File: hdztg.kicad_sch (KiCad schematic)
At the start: 8 parts, among them J1 20374-R20E-31, Q1 2N7002KDW 72K

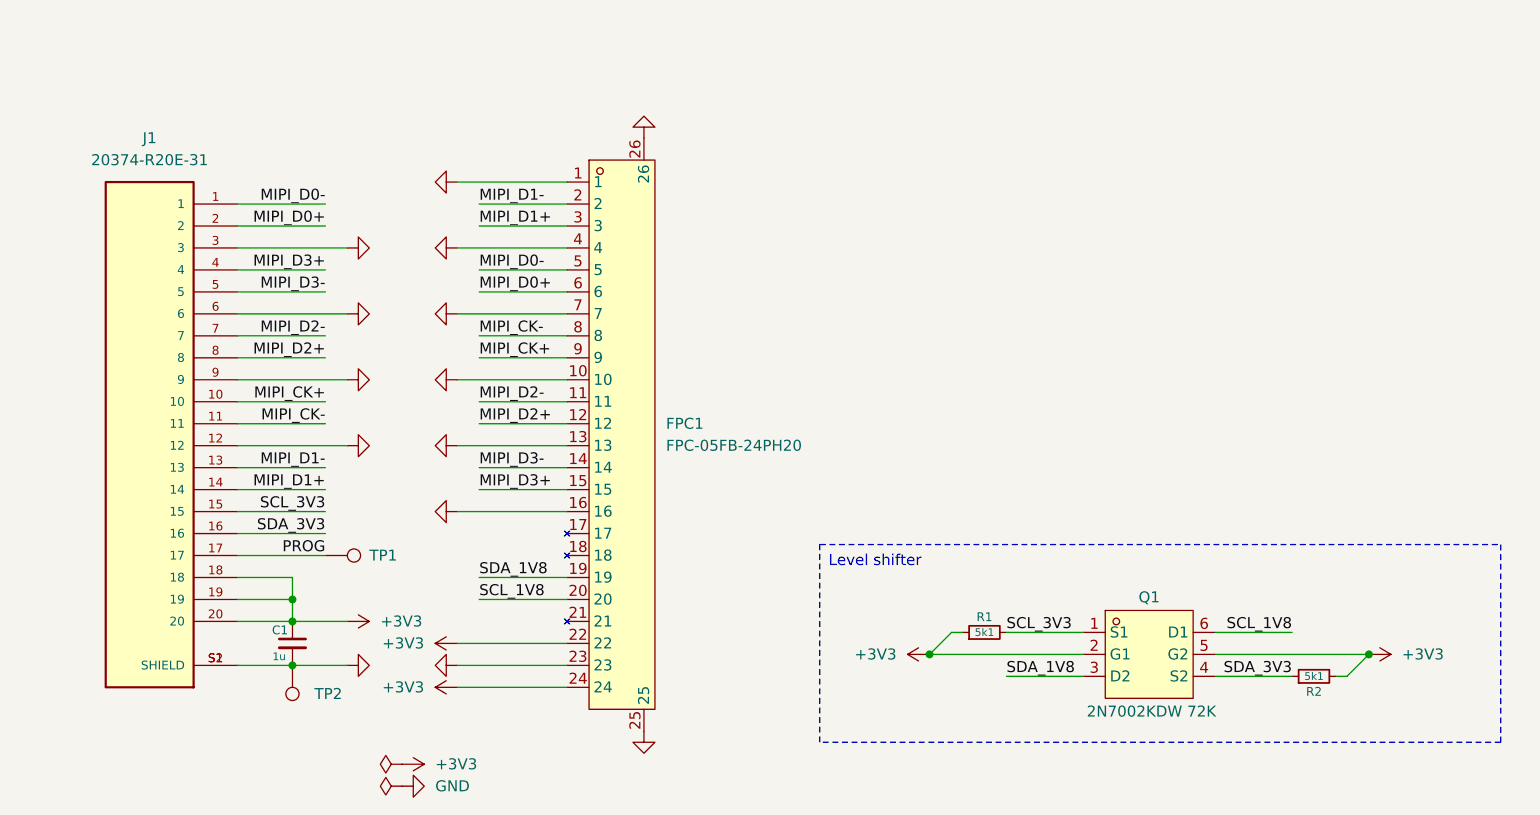
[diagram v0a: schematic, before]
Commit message: update pcb, fix level shifter
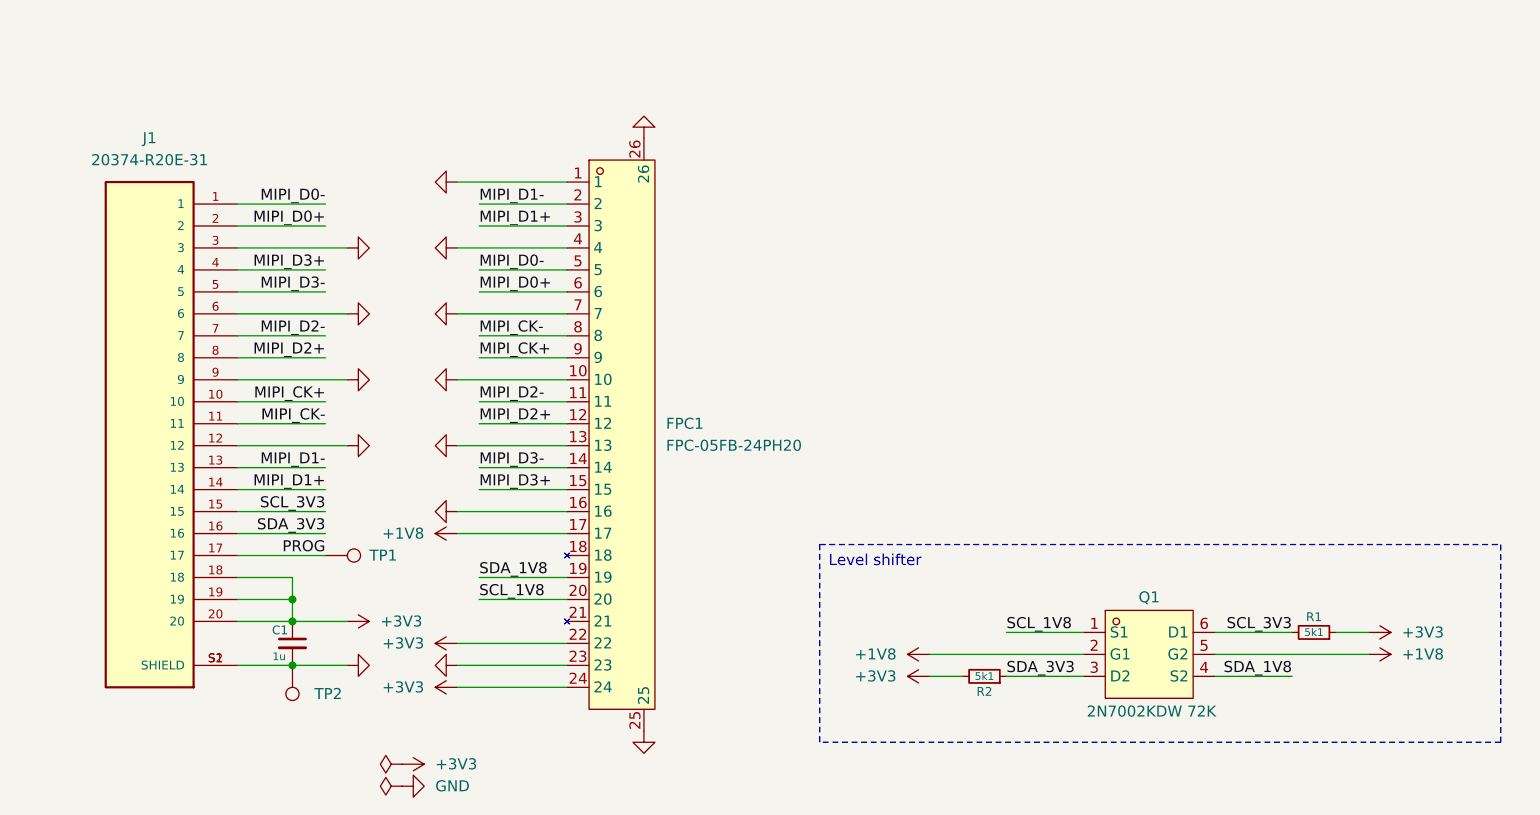
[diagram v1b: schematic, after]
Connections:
- net +3V3: no longer Q1.2 (G1), Q1.5 (G2)
- net SCL_1V8: now also Q1.1 (S1); no longer Q1.6 (D1)
- net SCL_3V3: now also Q1.6 (D1); no longer Q1.1 (S1)
- net SDA_1V8: now also Q1.4 (S2); no longer Q1.3 (D2)
- net SDA_3V3: now also Q1.3 (D2); no longer Q1.4 (S2)
- net +1V8: now reaches FPC1.17
- net +1V8: now also Q1.2 (G1), Q1.5 (G2)
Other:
- moved on the sheet: R1, R2

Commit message: update pcb
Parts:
- FPC1: Manufacturer Part (none) -> FPC-05FB-24PH20; Supplier Link (none) -> https://lcsc.com/product-detail/FFC-FPC-Flat-Flexible-Conne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
- J1: Availability In Stock -> (none); Check_prices https://www.snapeda.com/parts/20374-R20E-31/I-PEX/view-part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 -> (none); Description_1 20 POS Right Angle SMD 0.4 mm pitch vertical mating type mi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 -> (none); DigiKey Part (none) -> 5378-20374-R20E-31TR-ND; MANUFACTURER I-PEX -> (none); MF I-PEX -> (none); MP 20374-R20E-31 -> (none); Manufacturer (none) -> I-PEX; Manufacturer Product Number (none) -> 20374-R20E-31; PARTREV 24 -> (none); Package None -> (none); Price None -> (none); STANDARD Manufacturer Recommendation -> (none); SnapEDA_Link https://www.snapeda.com/parts/20374-R20E-31/I-PEX/view-part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 -> (none); Supplier Link (none) -> https://www.digikey.com/en/products/detail/i-pex/20374-R20E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
- Q1: Manufacturer Part (none) -> 2N7002KDW; Supplier Link (none) -> https://lcsc.com/product-detail/MOSFETs_CBI-2N7002KDW_C2919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
- R1, R2: LCSC Part (none) -> C274341; Manufacturer Part (none) -> RC0201FR-075K1L; Supplier Link (none) -> https://lcsc.com/product-detail/Chip-Resistor-Surface-Mount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
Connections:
- net +3V3: now also R1.2; no longer R1.1
- net SCL_3V3: now also R1.1; no longer R1.2
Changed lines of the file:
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@@
 			)
 		)
-		(property "Datasheet" ""
+		(property "Datasheet" "https://www.i-pex.com/sites/default/files/downloads/pdf/CATALOG_CABLINE-SS_E.pdf"
 			(at 35.56 62.23 0)
 			(effects
@@
 			)
 		)
-		(property "Description" ""
+		(property "Description" "20 POS Right Angle SMD 0.4 mm pitch vertical mating type micro-coaxial connector with friction lock CABLINE SS Receptacle"
 			(at 35.56 62.23 0)
 			(effects
@@
 			)
 		)
-		(property "MF" "I-PEX"
+		(property "Manufacturer Product Number" "20374-R20E-31"
 			(at 35.56 62.23 0)
 			(effects
@@
 			)
 		)
-		(property "Description_1" "20 POS Right Angle SMD 0.4 mm pitch vertical mating type micro-coaxial connector with friction lock CABLINE SS Receptacle"
+		(property "Manufacturer" "I-PEX"
 			(at 35.56 62.23 0)
 			(effects
@@
 			)
 		)
-		(property "Package" "None"
+		(property "DigiKey Part" "5378-20374-R20E-31TR-ND"
 			(at 35.56 62.23 0)
 			(effects
@@
 					(size 1.27 1.27)
 				)
-				(justify bottom)
-				(hide yes)
-			)
-		)
-		(property "Price" "None"
+				(hide yes)
+			)
+		)
+		(property "Supplier Link" "https://www.digikey.com/en/products/detail/i-pex/20374-R20E-31/24394701"
 			(at 35.56 62.23 0)
 			(effects
@@
 					(size 1.27 1.27)
 				)
-				(justify bottom)
-				(hide yes)
-			)
-		)
-		(property "Check_prices" "https://www.snapeda.com/parts/20374-R20E-31/I-PEX/view-part/?ref=eda"
-			(at 35.56 62.23 0)
-			(effects
-				(font
-					(size 1.27 1.27)
-				)
-				(justify bottom)
-				(hide yes)
-			)
-		)
-		(property "STANDARD" "Manufacturer Recommendation"
-			(at 35.56 62.23 0)
-			(effects
-				(font
-					(size 1.27 1.27)
-				)
-				(justify bottom)
-				(hide yes)
-			)
-		)
-		(property "PARTREV" "24"
-			(at 35.56 62.23 0)
-			(effects
-				(font
-					(size 1.27 1.27)
-				)
-				(justify bottom)
-				(hide yes)
-			)
-		)
-		(property "SnapEDA_Link" "https://www.snapeda.com/parts/20374-R20E-31/I-PEX/view-part/?ref=snap"
-			(at 35.56 62.23 0)
-			(effects
-				(font
-					(size 1.27 1.27)
-				)
-				(justify bottom)
-				(hide yes)
-			)
-		)
-		(property "MP" "20374-R20E-31"
-			(at 35.56 62.23 0)
-			(effects
-				(font
-					(size 1.27 1.27)
-				)
-				(justify bottom)
-				(hide yes)
-			)
-		)
-		(property "Availability" "In Stock"
-			(at 35.56 62.23 0)
-			(effects
-				(font
-					(size 1.27 1.27)
-				)
-				(justify bottom)
-				(hide yes)
-			)
-		)
-		(property "MANUFACTURER" "I-PEX"
-			(at 35.56 62.23 0)
-			(effects
-				(font
-					(size 1.27 1.27)
-				)
-				(justify bottom)
 				(hide yes)
 			)
@@
 			)
 		)
+		(property "Manufacturer Part" "2N7002KDW"
+			(at 151.13 88.9 0)
+			(effects
+				(font
+					(size 1.27 1.27)
+				)
+				(hide yes)
+			)
+		)
 		(property "LCSC Part" "C2919800"
 			(at 151.13 101.6 0)
+			(effects
+				(font
+					(size 1.27 1.27)
+				)
+				(hide yes)
+			)
+		)
+		(property "Supplier Link" "https://lcsc.com/product-detail/MOSFETs_CBI-2N7002KDW_C2919800.html?s_z=n_2N7002KDW"
+			(at 151.13 88.9 0)
 			(effects
 				(font
@@
 	)
 	(symbol
+		(lib_id "Device:R_Small")
+		(at 170.18 86.36 90)
+		(mirror x)
+		(unit 1)
+		(exclude_from_sim no)
+		(in_bom yes)
+		(on_board yes)
+		(dnp no)
+		(property "Reference" "R1"
+			(at 170.18 84.582 90)
+			(effects
+				(font
+					(size 1.016 1.016)
+				)
+			)
+		)
+		(property "Value" "5k1"
+			(at 170.18 86.36 90)
+			(effects
+				(font
+					(size 0.889 0.889)
+				)
+			)
+		)
+		(property "Footprint" "Resistor_SMD:R_0201_0603Metric"
+			(at 170.18 86.36 0)
+			(effects
+				(font
+					(size 1.27 1.27)
+				)
+				(hide yes)
+			)
+		)
+		(property "Datasheet" "https://lcsc.com/datasheet/lcsc_datasheet_2506161045_YAGEO-RC0201FR-075K1L_C274341.pdf"
+			(at 170.18 86.36 0)
+			(effects
+				(font
+					(size 1.27 1.27)
+				)
+				(hide yes)
+			)
+		)
+		(property "Description" "Resistor, small symbol"
+			(at 170.18 86.36 0)
+			(effects
+				(font
+					(size 1.27 1.27)
+				)
+				(hide yes)
+			)
+		)
+		(property "Manufacturer Part" "RC0201FR-075K1L"
+			(at 170.18 86.36 90)
+			(effects
+				(font
+					(size 1.27 1.27)
+				)
+				(hide yes)
+			)
+		)
+		(property "LCSC Part" "C274341"
+			(at 170.18 86.36 90)
+			(effects
+				(font
+					(size 1.27 1.27)
+				)
+				(hide yes)
+			)
+		)
+		(property "Supplier Link" "https://lcsc.com/product-detail/Chip-Resistor-Surface-Mount_YAGEO-RC0201FR-075K1L_C274341.html"
+			(at 170.18 86.36 90)
+			(effects
+				(font
+					(size 1.27 1.27)
+				)
+				(hide yes)
+			)
+		)
+		(pin "1"
+		)
+		(pin "2"
+		)
+		(instances
+			(project "hdztg"
+				(path "/5fa3be86-0836-40c5-8497-58cbc35ea59a"
+					(reference "R1")
+					(unit 1)
+				)
+			)
+		)
+	)
+	(symbol
 		(lib_id "power:GND")
 		(at 58.42 41.91 90)
@@
 				(path "/5fa3be86-0836-40c5-8497-58cbc35ea59a"
 					(reference "#PWR015")
-					(unit 1)
-				)
-			)
-		)
-	)
-	(symbol
-		(lib_id "Device:R_Small")
-		(at 170.18 86.36 270)
-		(mirror x)
-		(unit 1)
-		(exclude_from_sim no)
-		(in_bom yes)
-		(on_board yes)
-		(dnp no)
-		(property "Reference" "R1"
-			(at 170.18 84.582 90)
-			(effects
-				(font
-					(size 1.016 1.016)
-				)
-			)
-		)
-		(property "Value" "5k1"
-			(at 170.18 86.36 90)
-			(effects
-				(font
-					(size 0.889 0.889)
-				)
-			)
-		)
-		(property "Footprint" "Resistor_SMD:R_0201_0603Metric"
-			(at 170.18 86.36 0)
-			(effects
-				(font
-					(size 1.27 1.27)
-				)
-				(hide yes)
-			)
-		)
-		(property "Datasheet" "~"
-			(at 170.18 86.36 0)
-			(effects
-				(font
-					(size 1.27 1.27)
-				)
-				(hide yes)
-			)
-		)
-		(property "Description" "Resistor, small symbol"
-			(at 170.18 86.36 0)
-			(effects
-				(font
-					(size 1.27 1.27)
-				)
-				(hide yes)
-			)
-		)
-		(pin "1"
-		)
-		(pin "2"
-		)
-		(instances
-			(project "hdztg"
-				(path "/5fa3be86-0836-40c5-8497-58cbc35ea59a"
-					(reference "R1")
 					(unit 1)
 				)
@@
 			)
 		)
-		(property "Datasheet" "~"
+		(property "Datasheet" "https://lcsc.com/datasheet/lcsc_datasheet_2506161045_YAGEO-RC0201FR-075K1L_C274341.pdf"
 			(at 132.08 91.44 0)
 			(effects
@@
 			)
 		)
+		(property "Manufacturer Part" "RC0201FR-075K1L"
+			(at 132.08 91.44 90)
+			(effects
+				(font
+					(size 1.27 1.27)
+				)
+				(hide yes)
+			)
+		)
+		(property "LCSC Part" "C274341"
+			(at 132.08 91.44 90)
+			(effects
+				(font
+					(size 1.27 1.27)
+				)
+				(hide yes)
+			)
+		)
+		(property "Supplier Link" "https://lcsc.com/product-detail/Chip-Resistor-Surface-Mount_YAGEO-RC0201FR-075K1L_C274341.html"
+			(at 132.08 91.44 90)
+			(effects
+				(font
+					(size 1.27 1.27)
+				)
+				(hide yes)
+			)
+		)
 		(pin "1"
 		)
@@
 			)
 		)
-		(property "Datasheet" ""
+		(property "Datasheet" "https://lcsc.com/datasheet/lcsc_datasheet_2411121000_XUNPU-FPC-05FB-24PH20_C2856831.pdf"
 			(at 88.9 63.5 0)
 			(effects
@@
 			)
 		)
-		(property "Description" ""
+		(property "Description" "Hinged Lid -25℃~+85℃ 24P Double-Sided Contacts, Top and Bottom Entry Surface Mount, Right Angle 0.5mm SMD,P=0.5mm,Surface Mount,Right Angle FFC, FPC (Flat Flexible) Connector Assemblies ROHS"
+			(at 88.9 63.5 0)
+			(effects
+				(font
+					(size 1.27 1.27)
+				)
+				(hide yes)
+			)
+		)
+		(property "Manufacturer Part" "FPC-05FB-24PH20"
 			(at 88.9 63.5 0)
 			(effects
@@
 			(effects
 				(font
+					(size 1.27 1.27)
+				)
+				(hide yes)
+			)
+		)
+		(property "Supplier Link" "https://lcsc.com/product-detail/FFC-FPC-Flat-Flexible-Connector-Assemblies_XUNPU-FPC-05FB-24PH20_C2856831.html?s_z=n_FPC-05FB-24PH20"
+			(at 88.9 63.5 0)
+			(effects
+				(font

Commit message: prod
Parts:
- removed Q1: 2N7002KDW 72K, EasyEDA:SOT-363_L2.1-W1.3-P0.65-LS2.3-BL, symbol EasyEDA:2N7002KDW72K
- removed TP1, TP2: TestPoint, TestPoint:TestPoint_Pad_D1.0mm, symbol Connector:TestPoint
- added Q2: BSS138DW-7-F, EasyEDA:SC-70-6_L2.2-W1.3-P0.65-LS2.1-TL, symbol EasyEDA:BSS138DW-7-F
- C1: Distributor Link (none) -> https://lcsc.com/product-detail/Multilayer-Ceramic-Capacito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; LCSC (none) -> C307385; Manufacturer Part (none) -> CL03A105MO3NRNH
- J1: Distributor Link (none) -> https://www.digikey.com/en/products/detail/i-pex/20374-R20E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; Manufacturer Part (none) -> 20374-R20E-31; Manufacturer Product Number 20374-R20E-31 -> (none); Supplier Link https://www.digikey.com/en/products/detail/i-pex/20374-R20E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 -> (none)
- J2: renamed from FPC1; Distributor Link (none) -> https://lcsc.com/product-detail/FFC-FPC-Flat-Flexible-Conne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; LCSC (none) -> C2856831; LCSC Part C2856831 -> (none); Supplier Link https://lcsc.com/product-detail/FFC-FPC-Flat-Flexible-Conne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 -> (none)
- R1, R2: Distributor Link (none) -> https://lcsc.com/product-detail/Chip-Resistor-Surface-Mount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; LCSC (none) -> C274341; LCSC Part C274341 -> (none); Supplier Link https://lcsc.com/product-detail/Chip-Resistor-Surface-Mount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 -> (none)
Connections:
- net +1V8: now also J2.8 (17), Q2.2 (G2), Q2.5 (G1); no longer J2.17
- net +3V3: now also J2.1 (24), J2.3 (22); no longer J2.22, J2.24
- net GND: now also J2.12 (13), J2.15 (10), J2.18 (7), J2.2 (23), J2.21 (4), J2.24 (1), J2.9 (16); no longer J2.1, J2.10, J2.13, J2.16, J2.23, J2.4, J2.7
- net MIPI_CK+: now also J2.16 (9); no longer J2.9
- net MIPI_CK-: now also J2.17 (8); no longer J2.8
- net MIPI_D0+: now also J2.19 (6); no longer J2.6
- net MIPI_D0-: now also J2.20 (5); no longer J2.5
- net MIPI_D1+: now also J2.22 (3); no longer J2.3
- net MIPI_D1-: now also J2.23 (2); no longer J2.2
- net MIPI_D2+: now also J2.13 (12); no longer J2.12
- net MIPI_D2-: now also J2.14 (11); no longer J2.11
- net MIPI_D3+: now also J2.10 (15); no longer J2.15
- net MIPI_D3-: now also J2.11 (14); no longer J2.14
- net SCL_1V8: now also J2.5 (20), Q2.4 (S1); no longer J2.20
- net SCL_3V3: now also Q2.3 (D1)
- net SDA_1V8: now also J2.6 (19), Q2.1 (S2); no longer J2.19
- net SDA_3V3: now also Q2.6 (D2)
- no-connect marks 0 -> 3
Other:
- note added: "(!) Pins are flipped Be careful"
- company: (none) -> Sigma Logic
- title: (none) -> HDZero Camera To Sipeed Board MIPI adapter
- moved on the sheet: C1, J1, R1, R2

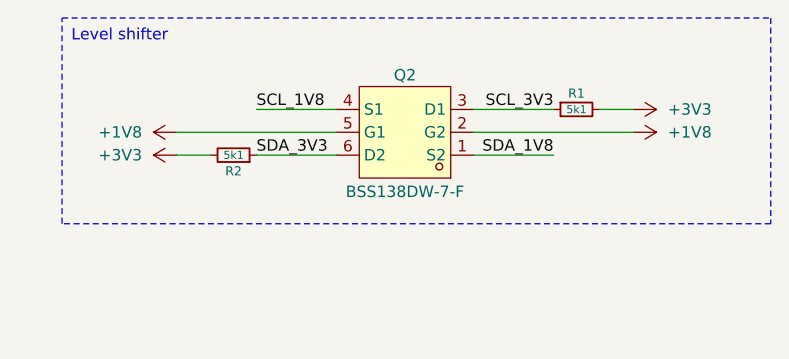
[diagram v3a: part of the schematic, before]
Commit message: fix bottom reference stitching
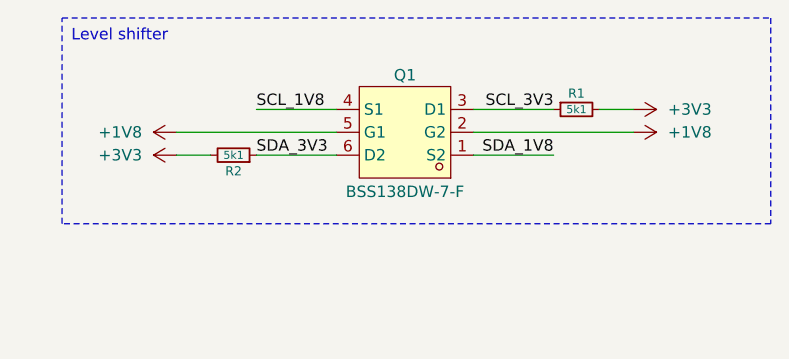
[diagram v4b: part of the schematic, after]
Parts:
- renumbered Q2 to Q1
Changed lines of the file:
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@@
 		(on_board yes)
 		(dnp no)
-		(property "Reference" "Q2"
+		(property "Reference" "Q1"
 			(at 153.67 21.59 0)
 			(effects
@@
 			(project ""
 				(path "/5fa3be86-0836-40c5-8497-58cbc35ea59a"
-					(reference "Q2")
+					(reference "Q1")
 					(unit 1)
 				)
